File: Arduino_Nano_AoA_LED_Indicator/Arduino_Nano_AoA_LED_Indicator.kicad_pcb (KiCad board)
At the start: 2 copper layers, 20 parts

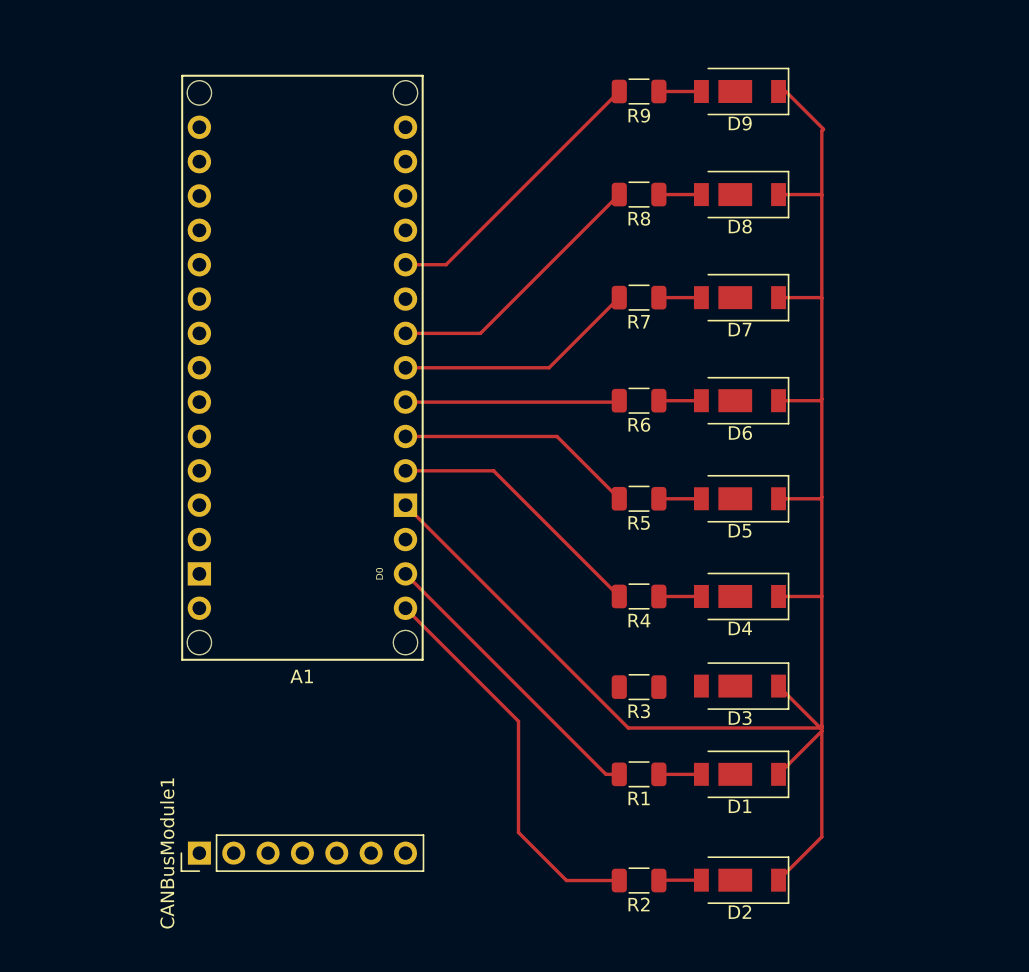
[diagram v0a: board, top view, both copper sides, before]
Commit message: Split the AOA LED project into two projects - one for the LEDs and one for the Nano board and the MCP2515 CAN board.
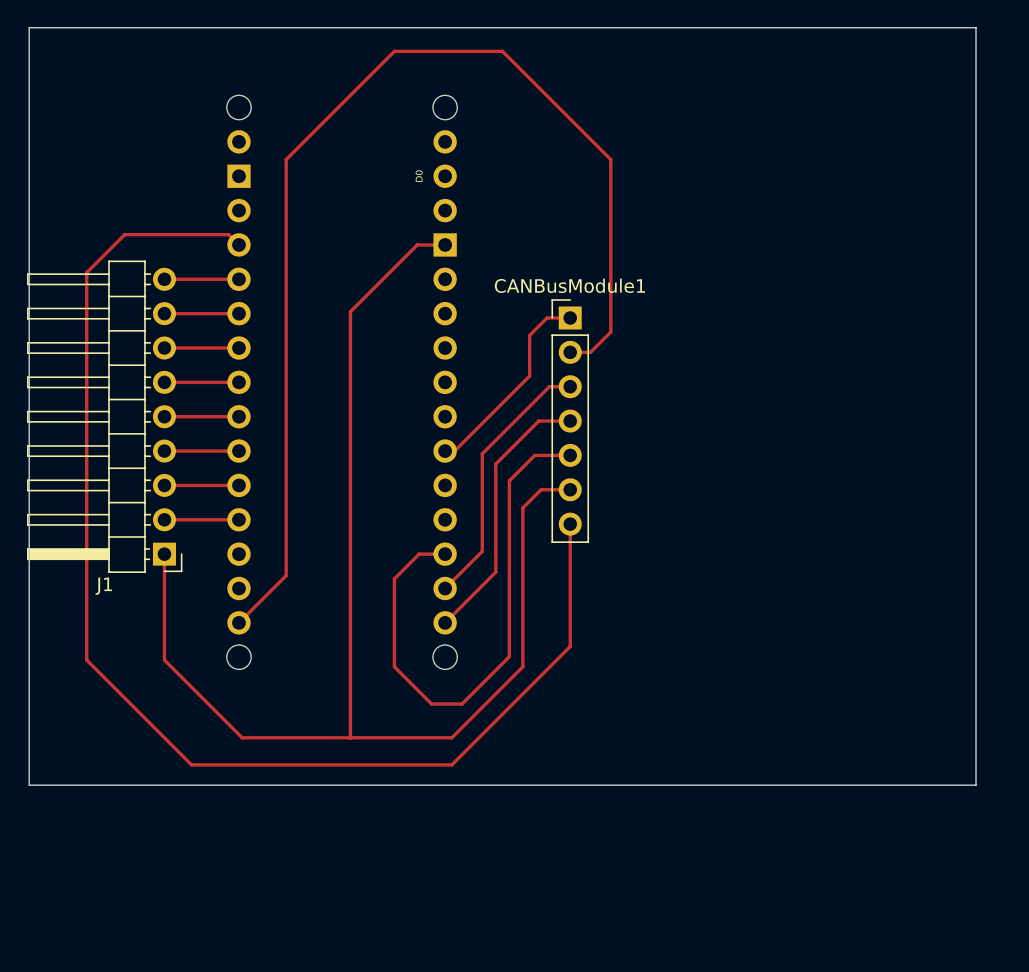
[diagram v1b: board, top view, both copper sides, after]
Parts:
- removed D1, D2, D3, D4, D5, D6, D7, D8, D9: LED, LED_SMD:LED_Yuji_5730
- removed R1, R2, R3, R4, R5, R6, R7, R8, R9: R, Resistor_SMD:R_1206_3216Metric
- added J1: Conn_01x09_Pin, Connector_PinHeader_2.54mm:PinHeader_1x09_P2.54mm_Horizontal, F.Cu at (84.8, 102.9)
- A1: moved to B.Cu
- moved CANBusModule1 48.1 mm to (114.8, 85.5), turned to 0 degrees
- moved A1 44.4 mm to (97.9, 111.8)
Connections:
- A1 pad A1: unconnected-(A1-PadA1) -> Net-(J1-Pin_3)
- A1 pad A2: unconnected-(A1-PadA2) -> Net-(J1-Pin_4)
- A1 pad A3: unconnected-(A1-PadA3) -> Net-(J1-Pin_5)
- A1 pad A4: unconnected-(A1-A4/SDA-PadA4) -> Net-(A1-A4/SDA)
- A1 pad A5: unconnected-(A1-A5/SCL-PadA5) -> Net-(A1-A5/SCL)
- A1 pad A6: unconnected-(A1-PadA6) -> Net-(J1-Pin_8)
- A1 pad A7: unconnected-(A1-PadA7) -> Net-(J1-Pin_9)
- A1 pad D0: Net-(A1-D0/RX) -> unconnected-(A1-D0/RX-PadD0)
- A1 pad D1: Net-(A1-D1/TX) -> unconnected-(A1-D1/TX-PadD1)
- A1 pad D2: Net-(A1-D2_INT0) -> unconnected-(A1-D2_INT0-PadD2)
- A1 pad D3: Net-(A1-D3_INT1) -> unconnected-(A1-D3_INT1-PadD3)
- A1 pad D4: Net-(A1-PadD4) -> unconnected-(A1-PadD4)
- A1 pad D5: Net-(A1-PadD5) -> unconnected-(A1-PadD5)
- A1 pad D6: Net-(A1-PadD6) -> unconnected-(A1-PadD6)
- A1 pad D8: Net-(A1-PadD8) -> unconnected-(A1-PadD8)
- A1 pad GND1: Net-(D1-K) -> Net-(CANBusModule1-Pin_6)
- A1 pad GND2: Net-(CANBusModule1-Pin_6) -> unconnected-(A1-GND-PadGND2)
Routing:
- net Net-(D1-K): track 124.3 -> 0.00 mm
- net Net-(CANBusModule1-Pin_6): track 0.00 -> 95.2 mm
- net Net-(CANBusModule1-Pin_7): track 0.00 -> 93.0 mm
- net Net-(A1-D13_SCK): track 0.00 -> 82.7 mm
- net Net-(CANBusModule1-Pin_5): track 0.00 -> 40.4 mm
- net Net-(A1-D1/TX): track 29.0 -> 0.00 mm
- net Net-(A1-D0/RX): track 21.9 -> 0.00 mm
- net Net-(A1-PadD8): track 21.1 -> 0.00 mm
- net Net-(A1-D12_MISO): track 0.00 -> 20.1 mm
- net Net-(A1-PadD6): track 20.1 -> 0.00 mm
- net Net-(A1-D11_MOSI): track 0.00 -> 19.7 mm
- net Net-(A1-D2_INT0): track 19.7 -> 0.00 mm
- net Net-(A1-PadD5): track 18.0 -> 0.00 mm
- net Net-(A1-D3_INT1): track 17.7 -> 0.00 mm
- net Net-(A1-PadD4): track 15.8 -> 0.00 mm
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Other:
- board outline added: 70 x 56 mm

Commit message: Created a new board for the Wit-Motion WT901B IMU chip.
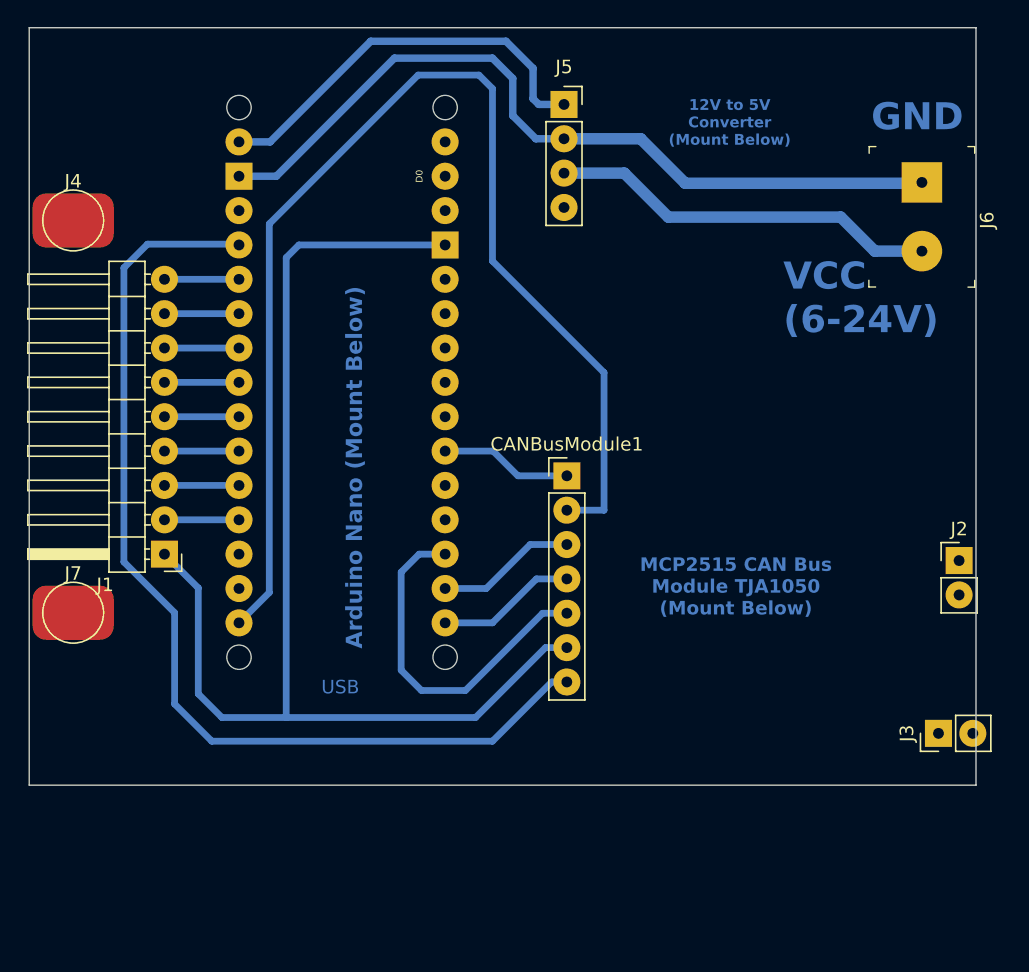
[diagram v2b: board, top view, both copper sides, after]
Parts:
- added J2: Conn_01x02_Pin, Connector_PinHeader_2.54mm:PinHeader_1x02_P2.54mm_Vertical, F.Cu at (143.5, 103.4)
- added J3: Conn_01x02_Pin, Connector_PinHeader_2.54mm:PinHeader_1x02_P2.54mm_Vertical, F.Cu at (142.0, 116.2)
- added J4: SolderPad1, TestPoint:TestPoint_Pad_D4.0mm, F.Cu at (78.0, 78.2)
- added J5: Conn_01x04, Connector_PinSocket_2.54mm:PinSocket_1x04_P2.54mm_Vertical, F.Cu at (114.3, 69.7)
- added J6: OSTTC022162, digikey-footprints:Term_Block_1x2_P5.08MM, F.Cu at (140.8, 75.4)
- added J7: SolderPad2, TestPoint:TestPoint_Pad_D4.0mm, F.Cu at (78.0, 107.2)
- moved CANBusModule1 11.7 mm to (114.5, 97.1)
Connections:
- A1 pad GND2: unconnected-(A1-GND-PadGND2) -> GND
- A1 pad VIN: unconnected-(A1-PadVIN) -> Net-(J5-Pin_1)
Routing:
- net GND: track 0.00 -> 58.9 mm
- net Net-(J5-Pin_1): track 0.00 -> 30.4 mm
- net +12V: track 0.00 -> 28.1 mm
- net Net-(CANBusModule1-Pin_7): track 93.0 -> 75.0 mm
- net Net-(CANBusModule1-Pin_5): track 40.4 -> 26.3 mm
- net Net-(A1-D12_MISO): track 20.1 -> 10.3 mm
- net Net-(A1-D11_MOSI): track 19.7 -> 10.3 mm
- net Net-(CANBusModule1-Pin_6): track 95.2 -> 87.6 mm
- net Net-(A1-D13_SCK): track 82.7 -> 89.2 mm
- net Net-(CANBusModule1-Pin_1): track 15.1 -> 10.9 mm
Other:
- board text added: "12V to 5V Converter (Mount Below)"
- board text added: "Arduino Nano (Mount Below)"
- board text added: "GND"
- board text added: "MCP2515 CAN Bus Module TJA1050 (Mount Below)"
- board text added: "USB"
- board text added: "VCC (6-24V)"
